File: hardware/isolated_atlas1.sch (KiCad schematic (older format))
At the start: 17 parts, among them J301 CONN_01X02, P3 ATLAS_RTD_PROBE, U301 ADM3260, U302 ATLAS_RTD

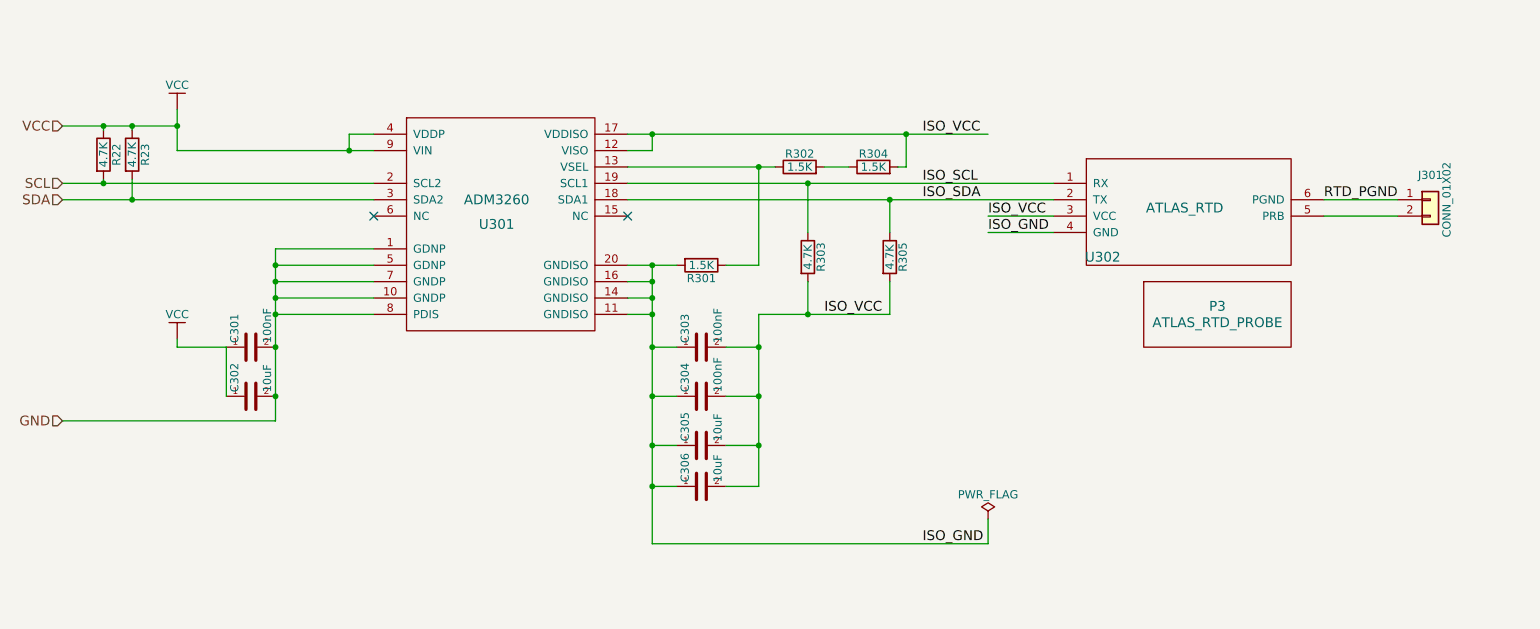
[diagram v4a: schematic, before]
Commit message: Generated panelized version of v0.11, including gerbers
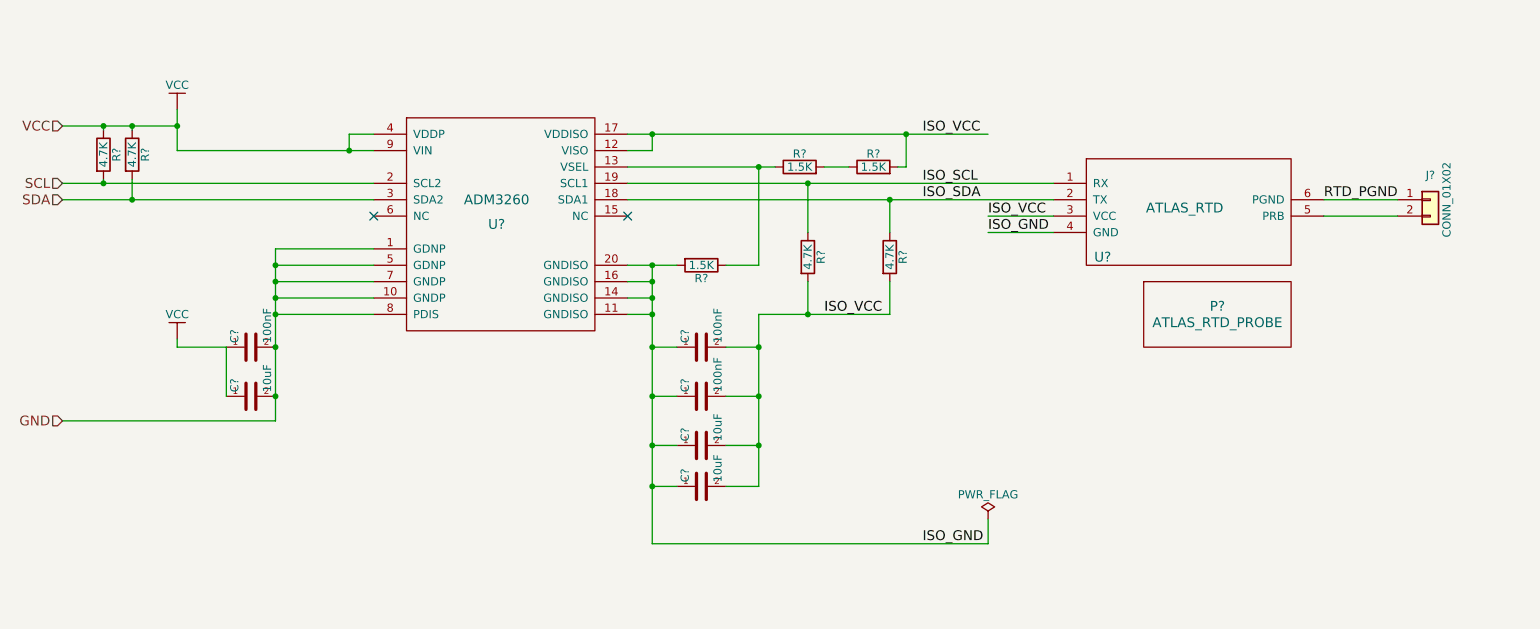
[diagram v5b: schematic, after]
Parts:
- renumbered C305 to C?, C303 to C?, C304 to C?, C306 to C?, C301 to C?, C302 to C?, J301 to J?, P3 to P?, R305 to R?, R301 to R?, R302 to R?, R304 to R?, R303 to R?, R22 to R?, R23 to R?, U301 to U?, U302 to U?
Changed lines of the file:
@@
 $EndDescr
 $Comp
-L fk-atlas-rescue:ADM3260-conservify U301
+L fk-atlas-rescue:ADM3260-conservify U?
 U 1 1 594C2CF2
 P 4400 2900
-F 0 "U301" H 4400 2750 60  0000 C CNN
+F 0 "U?" H 4400 2750 60  0000 C CNN
 F 1 "ADM3260" H 4400 2900 60  0000 C CNN
 F 2 "conservify:SSOP20-53" H 4400 2900 60  0001 C CNN
@@
 $EndComp
 $Comp
-L fk-atlas-rescue:CAPACITOR_CERAMIC-conservify C303
+L fk-atlas-rescue:CAPACITOR_CERAMIC-conservify C?
 U 1 1 594C2CF6
 P 5650 3800
-F 0 "C303" H 5675 3900 50  0000 L CNN
+F 0 "C?" H 5675 3900 50  0000 L CNN
 F 1 "100nF" H 5675 3700 50  0000 L CNN
 F 2 "conservify:CAP-0603" H 5688 3650 50  0001 C CNN
@@
 $EndComp
 $Comp
-L fk-atlas-rescue:CAPACITOR_CERAMIC-conservify C304
+L fk-atlas-rescue:CAPACITOR_CERAMIC-conservify C?
 U 1 1 594C2CF7
 P 5650 4100
-F 0 "C304" H 5675 4200 50  0000 L CNN
+F 0 "C?" H 5675 4200 50  0000 L CNN
 F 1 "100nF" H 5675 4000 50  0000 L CNN
 F 2 "conservify:CAP-0603" H 5688 3950 50  0001 C CNN
@@
 $EndComp
 $Comp
-L fk-atlas-rescue:CAPACITOR_CERAMIC-conservify C305
+L fk-atlas-rescue:CAPACITOR_CERAMIC-conservify C?
 U 1 1 5948D5A8
 P 5650 4400
-F 0 "C305" H 5675 4500 50  0000 L CNN
+F 0 "C?" H 5675 4500 50  0000 L CNN
 F 1 "10uF" H 5675 4300 50  0000 L CNN
 F 2 "conservify:CAP-0603" H 5688 4250 50  0001 C CNN
@@
 $EndComp
 $Comp
-L fk-atlas-rescue:CAPACITOR_CERAMIC-conservify C306
+L fk-atlas-rescue:CAPACITOR_CERAMIC-conservify C?
 U 1 1 594C2D02
 P 5650 4650
-F 0 "C306" H 5675 4750 50  0000 L CNN
+F 0 "C?" H 5675 4750 50  0000 L CNN
 F 1 "10uF" H 5675 4550 50  0000 L CNN
 F 2 "conservify:CAP-0603" H 5688 4500 50  0001 C CNN
@@
 $EndComp
 $Comp
-L fk-atlas-rescue:CAPACITOR_CERAMIC-conservify C301
+L fk-atlas-rescue:CAPACITOR_CERAMIC-conservify C?
 U 1 1 594C2D04
 P 2900 3800
-F 0 "C301" H 2925 3900 50  0000 L CNN
+F 0 "C?" H 2925 3900 50  0000 L CNN
 F 1 "100nF" H 2925 3700 50  0000 L CNN
 F 2 "conservify:CAP-0603" H 2938 3650 50  0001 C CNN
@@
 $EndComp
 $Comp
-L fk-atlas-rescue:CAPACITOR_CERAMIC-conservify C302
+L fk-atlas-rescue:CAPACITOR_CERAMIC-conservify C?
 U 1 1 594C2D09
 P 2900 4100
-F 0 "C302" H 2925 4200 50  0000 L CNN
+F 0 "C?" H 2925 4200 50  0000 L CNN
 F 1 "10uF" H 2925 4000 50  0000 L CNN
 F 2 "conservify:CAP-0603" H 2938 3950 50  0001 C CNN
@@
 $EndComp
 $Comp
-L fk-atlas-rescue:R-conservify R301
+L fk-atlas-rescue:R-conservify R?
 U 1 1 594C2D0C
 P 5650 3300
-F 0 "R301" V 5730 3300 50  0000 C CNN
+F 0 "R?" V 5730 3300 50  0000 C CNN
 F 1 "1.5K" V 5650 3300 50  0000 C CNN
 F 2 "conservify:RES-0603" V 5580 3300 50  0001 C CNN
@@
 $EndComp
 $Comp
-L fk-atlas-rescue:R-conservify R302
+L fk-atlas-rescue:R-conservify R?
 U 1 1 594C2D0F
 P 6250 2700
-F 0 "R302" V 6330 2700 50  0000 C CNN
+F 0 "R?" V 6330 2700 50  0000 C CNN
 F 1 "1.5K" V 6250 2700 50  0000 C CNN
 F 2 "conservify:RES-0603" V 6180 2700 50  0001 C CNN
@@
 $EndComp
 $Comp
-L fk-atlas-rescue:R-conservify R304
+L fk-atlas-rescue:R-conservify R?
 U 1 1 594C2D16
 P 6700 2700
-F 0 "R304" V 6780 2700 50  0000 C CNN
+F 0 "R?" V 6780 2700 50  0000 C CNN
 F 1 "1.5K" V 6700 2700 50  0000 C CNN
 F 2 "conservify:RES-0603" V 6630 2700 50  0001 C CNN
@@
 $EndComp
 $Comp
-L fk-atlas-rescue:R-conservify R303
+L fk-atlas-rescue:R-conservify R?
 U 1 1 594C2D1A
 P 6300 3250
-F 0 "R303" V 6380 3250 50  0000 C CNN
+F 0 "R?" V 6380 3250 50  0000 C CNN
 F 1 "4.7K" V 6300 3250 50  0000 C CNN
 F 2 "conservify:RES-0603" V 6230 3250 50  0001 C CNN
@@
 $EndComp
 $Comp
-L fk-atlas-rescue:R-conservify R305
+L fk-atlas-rescue:R-conservify R?
 U 1 1 5948E4EE
 P 6800 3250
-F 0 "R305" V 6880 3250 50  0000 C CNN
+F 0 "R?" V 6880 3250 50  0000 C CNN
 F 1 "4.7K" V 6800 3250 50  0000 C CNN
 F 2 "conservify:RES-0603" V 6730 3250 50  0001 C CNN
@@
 $EndComp
 $Comp
-L fk-atlas-rescue:VCC-conservify #PWR059
+L fk-atlas-rescue:VCC-conservify #PWR?
 U 1 1 594C2D23
 P 2450 3750
-F 0 "#PWR059" H 2450 3600 50  0001 C CNN
+F 0 "#PWR?" H 2450 3600 50  0001 C CNN
 F 1 "VCC" H 2450 3900 50  0000 C CNN
 F 2 "" H 2450 3750 50  0001 C CNN
@@
 $EndComp
 $Comp
-L fk-atlas-rescue:VCC-conservify #PWR060
+L fk-atlas-rescue:VCC-conservify #PWR?
 U 1 1 594C2D29
 P 2450 2350
-F 0 "#PWR060" H 2450 2200 50  0001 C CNN
+F 0 "#PWR?" H 2450 2200 50  0001 C CNN
 F 1 "VCC" H 2450 2500 50  0000 C CNN
 F 2 "" H 2450 2350 50  0001 C CNN
@@
 $EndComp
 $Comp
-L fk-atlas-rescue:ATLAS_SENSOR-conservify U302
+L fk-atlas-rescue:ATLAS_SENSOR-conservify U?
 U 1 1 594C2D36
 P 8550 2900
-F 0 "U302" H 8100 2550 60  0000 C CNN
+F 0 "U?" H 8100 2550 60  0000 C CNN
 F 1 "ATLAS_RTD" H 8600 2850 60  0000 C CNN
 F 2 "conservify:ATLAS_SENSOR_BOARD_RTD_COMBO" H 8550 2900 60  0001 C CNN
@@
 $EndComp
 $Comp
-L fk-atlas-rescue:CONN_01x02-conservify J301
+L fk-atlas-rescue:CONN_01x02-conservify J?
 U 1 1 59A1BC7C
 P 10100 2900
-F 0 "J301" H 10100 3050 50  0000 C CNN
+F 0 "J?" H 10100 3050 50  0000 C CNN
 F 1 "CONN_01X02" V 10200 2900 50  0000 C CNN
 F 2 "conservify:BNC" H 10100 2900 50  0001 C CNN
@@
 $EndComp
 $Comp
-L fk-atlas-rescue:ATLAS_WATER_PROBE-conservify P3
+L fk-atlas-rescue:ATLAS_WATER_PROBE-conservify P?
 U 1 1 59D29DF5
 P 8800 3550
-F 0 "P3" H 8800 3550 60  0000 C CNN
+F 0 "P?" H 8800 3550 60  0000 C CNN
 F 1 "ATLAS_RTD_PROBE" H 8800 3450 60  0000 C CNN
 F 2 "conservify:Dummy_Empty" H 8800 3550 60  0001 C CNN
@@
 $EndComp
 $Comp
-L fk-atlas-rescue:PWR_FLAG-conservify #FLG0105
+L fk-atlas-rescue:PWR_FLAG-conservify #FLG?
 U 1 1 5BCBBD88
 P 7400 4850
-F 0 "#FLG0105" H 7400 4925 50  0001 C CNN
+F 0 "#FLG?" H 7400 4925 50  0001 C CNN
 F 1 "PWR_FLAG" H 7400 5000 50  0000 C CNN
 F 2 "" H 7400 4850 50  0001 C CNN
@@
 NoConn ~ 5200 3000
 $Comp
-L fk-atlas-rescue:R-conservify R22
+L fk-atlas-rescue:R-conservify R?
 U 1 1 5C7F5CBD
 P 2000 2625
-F 0 "R22" V 2080 2625 50  0000 C CNN
+F 0 "R?" V 2080 2625 50  0000 C CNN
 F 1 "4.7K" V 2000 2625 50  0000 C CNN
 F 2 "conservify:RES-0603" V 1930 2625 50  0001 C CNN
@@
 	2000 2800 3650 2800
 $Comp
-L fk-atlas-rescue:R-conservify R23
+L fk-atlas-rescue:R-conservify R?
 U 1 1 5C7F97D8
 P 2175 2625
-F 0 "R23" V 2255 2625 50  0000 C CNN
+F 0 "R?" V 2255 2625 50  0000 C CNN
 F 1 "4.7K" V 2175 2625 50  0000 C CNN
 F 2 "conservify:RES-0603" V 2105 2625 50  0001 C CNN
